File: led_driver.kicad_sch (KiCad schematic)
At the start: 4 parts, among them Q10 MMBT5551

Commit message: order files
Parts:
- renumbered R18 to R21
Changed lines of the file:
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@@
   (symbol (lib_id "Device:R") (at 74.93 45.72 90)
     (in_bom yes) (on_board yes)
-    (property "Reference" "R18" (id 0) (at 74.93 40.4622 90))
+    (property "Reference" "R21" (id 0) (at 74.93 40.4622 90))
     (property "Value" "4.7k" (id 1) (at 74.93 42.7736 90))
     (property "Footprint" "Resistor_SMD:R_0402_1005Metric" (id 2) (at 74.93 47.498 90)
@@
   (symbol (lib_id "power:GND") (at 76.2 53.34 90)
     (in_bom yes) (on_board yes)
-    (property "Reference" "#PWR039" (id 0) (at 82.55 53.34 0)
+    (property "Reference" "#PWR040" (id 0) (at 82.55 53.34 0)
       (effects (font (size 1.27 1.27)) hide)
     )

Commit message: rendered some docs
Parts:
- renumbered Q10 to Q9, R19 to R16, R20 to R17, R21 to R18
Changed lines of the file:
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@@
   (symbol (lib_id "Transistor_BJT:MMBT5551L") (at 71.12 50.8 90) (mirror x)
     (in_bom yes) (on_board yes)
-    (property "Reference" "Q10" (id 0) (at 71.12 56.769 90))
+    (property "Reference" "Q9" (id 0) (at 71.12 56.769 90))
     (property "Value" "MMBT5551" (id 1) (at 71.12 59.0804 90))
     (property "Footprint" "Package_TO_SOT_SMD:SOT-23" (id 2) (at 73.025 55.88 0)
@@
   (symbol (lib_id "Device:R") (at 74.93 45.72 90)
     (in_bom yes) (on_board yes)
-    (property "Reference" "R21" (id 0) (at 74.93 40.4622 90))
+    (property "Reference" "R18" (id 0) (at 74.93 40.4622 90))
     (property "Value" "4.7k" (id 1) (at 74.93 42.7736 90))
     (property "Footprint" "Resistor_SMD:R_0402_1005Metric" (id 2) (at 74.93 47.498 90)
@@
   (symbol (lib_id "power:GND") (at 76.2 53.34 90)
     (in_bom yes) (on_board yes)
-    (property "Reference" "#PWR040" (id 0) (at 82.55 53.34 0)
+    (property "Reference" "#PWR039" (id 0) (at 82.55 53.34 0)
       (effects (font (size 1.27 1.27)) hide)
     )
@@
   (symbol (lib_id "Device:R") (at 45.72 53.34 90)
     (in_bom yes) (on_board yes)
-    (property "Reference" "R19" (id 0) (at 45.72 48.0822 90))
+    (property "Reference" "R16" (id 0) (at 45.72 48.0822 90))
     (property "Value" "4.7k" (id 1) (at 45.72 50.3936 90))
     (property "Footprint" "Resistor_SMD:R_0402_1005Metric" (id 2) (at 45.72 55.118 90)
@@
   (symbol (lib_id "Device:R") (at 45.72 55.88 90)
     (in_bom yes) (on_board yes)
-    (property "Reference" "R20" (id 0) (at 45.72 58.801 90))
+    (property "Reference" "R17" (id 0) (at 45.72 58.801 90))
     (property "Value" "4.7k" (id 1) (at 45.72 61.1124 90))
     (property "Footprint" "Resistor_SMD:R_0402_1005Metric" (id 2) (at 45.72 57.658 90)

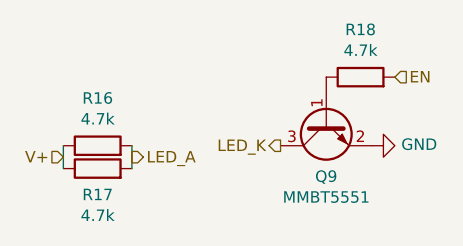
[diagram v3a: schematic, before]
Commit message: TVS diodes added to I2C SDA+SCL+INT pins, renamed 1-/2- to A-/B-
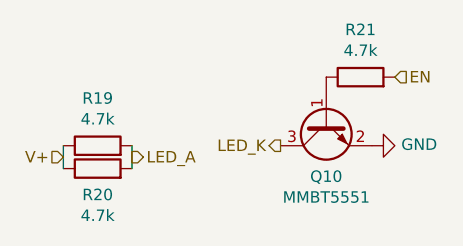
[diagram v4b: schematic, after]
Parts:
- renumbered Q9 to Q10, R16 to R19, R17 to R20, R18 to R21
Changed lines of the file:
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@@
   (symbol (lib_id "Transistor_BJT:MMBT5551L") (at 71.12 50.8 90) (mirror x)
     (in_bom yes) (on_board yes)
-    (property "Reference" "Q9" (id 0) (at 71.12 56.769 90))
+    (property "Reference" "Q10" (id 0) (at 71.12 56.769 90))
     (property "Value" "MMBT5551" (id 1) (at 71.12 59.0804 90))
     (property "Footprint" "Package_TO_SOT_SMD:SOT-23" (id 2) (at 73.025 55.88 0)
@@
   (symbol (lib_id "Device:R") (at 74.93 45.72 90)
     (in_bom yes) (on_board yes)
-    (property "Reference" "R18" (id 0) (at 74.93 40.4622 90))
+    (property "Reference" "R21" (id 0) (at 74.93 40.4622 90))
     (property "Value" "4.7k" (id 1) (at 74.93 42.7736 90))
     (property "Footprint" "Resistor_SMD:R_0402_1005Metric" (id 2) (at 74.93 47.498 90)
@@
   (symbol (lib_id "power:GND") (at 76.2 53.34 90)
     (in_bom yes) (on_board yes)
-    (property "Reference" "#PWR043" (id 0) (at 82.55 53.34 0)
+    (property "Reference" "#PWR047" (id 0) (at 82.55 53.34 0)
       (effects (font (size 1.27 1.27)) hide)
     )
@@
   (symbol (lib_id "Device:R") (at 45.72 53.34 90)
     (in_bom yes) (on_board yes)
-    (property "Reference" "R16" (id 0) (at 45.72 48.0822 90))
+    (property "Reference" "R19" (id 0) (at 45.72 48.0822 90))
     (property "Value" "4.7k" (id 1) (at 45.72 50.3936 90))
     (property "Footprint" "Resistor_SMD:R_0402_1005Metric" (id 2) (at 45.72 55.118 90)
@@
   (symbol (lib_id "Device:R") (at 45.72 55.88 90)
     (in_bom yes) (on_board yes)
-    (property "Reference" "R17" (id 0) (at 45.72 58.801 90))
+    (property "Reference" "R20" (id 0) (at 45.72 58.801 90))
     (property "Value" "4.7k" (id 1) (at 45.72 61.1124 90))
     (property "Footprint" "Resistor_SMD:R_0402_1005Metric" (id 2) (at 45.72 57.658 90)

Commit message: improvements, notes for future TODO stuff
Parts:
- renumbered Q10 to Q9, R19 to R16, R20 to R17, R21 to R18
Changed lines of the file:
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@@
   (symbol (lib_id "Transistor_BJT:MMBT5551L") (at 71.12 50.8 90) (mirror x)
     (in_bom yes) (on_board yes)
-    (property "Reference" "Q10" (id 0) (at 71.12 56.769 90))
+    (property "Reference" "Q9" (id 0) (at 71.12 56.769 90))
     (property "Value" "MMBT5551" (id 1) (at 71.12 59.0804 90))
     (property "Footprint" "Package_TO_SOT_SMD:SOT-23" (id 2) (at 73.025 55.88 0)
@@
   (symbol (lib_id "Device:R") (at 74.93 45.72 90)
     (in_bom yes) (on_board yes)
-    (property "Reference" "R21" (id 0) (at 74.93 40.4622 90))
+    (property "Reference" "R18" (id 0) (at 74.93 40.4622 90))
     (property "Value" "4.7k" (id 1) (at 74.93 42.7736 90))
     (property "Footprint" "Resistor_SMD:R_0402_1005Metric" (id 2) (at 74.93 47.498 90)
@@
   (symbol (lib_id "power:GND") (at 76.2 53.34 90)
     (in_bom yes) (on_board yes)
-    (property "Reference" "#PWR047" (id 0) (at 82.55 53.34 0)
+    (property "Reference" "#PWR046" (id 0) (at 82.55 53.34 0)
       (effects (font (size 1.27 1.27)) hide)
     )
@@
   (symbol (lib_id "Device:R") (at 45.72 53.34 90)
     (in_bom yes) (on_board yes)
-    (property "Reference" "R19" (id 0) (at 45.72 48.0822 90))
+    (property "Reference" "R16" (id 0) (at 45.72 48.0822 90))
     (property "Value" "4.7k" (id 1) (at 45.72 50.3936 90))
     (property "Footprint" "Resistor_SMD:R_0402_1005Metric" (id 2) (at 45.72 55.118 90)
@@
   (symbol (lib_id "Device:R") (at 45.72 55.88 90)
     (in_bom yes) (on_board yes)
-    (property "Reference" "R20" (id 0) (at 45.72 58.801 90))
+    (property "Reference" "R17" (id 0) (at 45.72 58.801 90))
     (property "Value" "4.7k" (id 1) (at 45.72 61.1124 90))
     (property "Footprint" "Resistor_SMD:R_0402_1005Metric" (id 2) (at 45.72 57.658 90)
